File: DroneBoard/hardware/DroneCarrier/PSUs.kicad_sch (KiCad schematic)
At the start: 33 parts, among them J7 Barrel_Jack, J8 AMP171826-4, Q1 DMP3013SFV-7, U6 AP64501SP-13

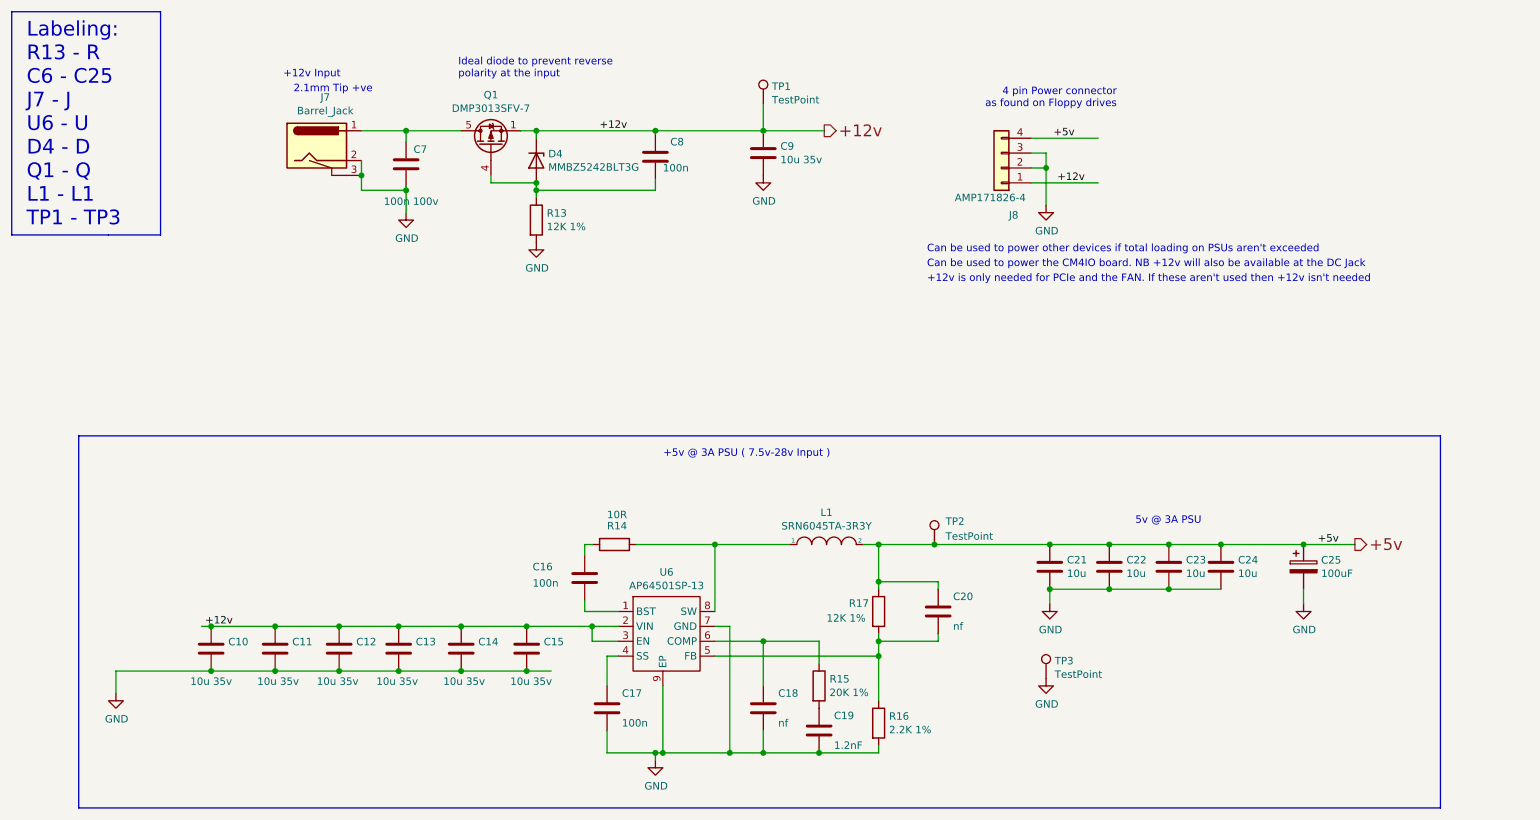
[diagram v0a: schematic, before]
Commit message: Labelling needs to be compared to the RPi CM4
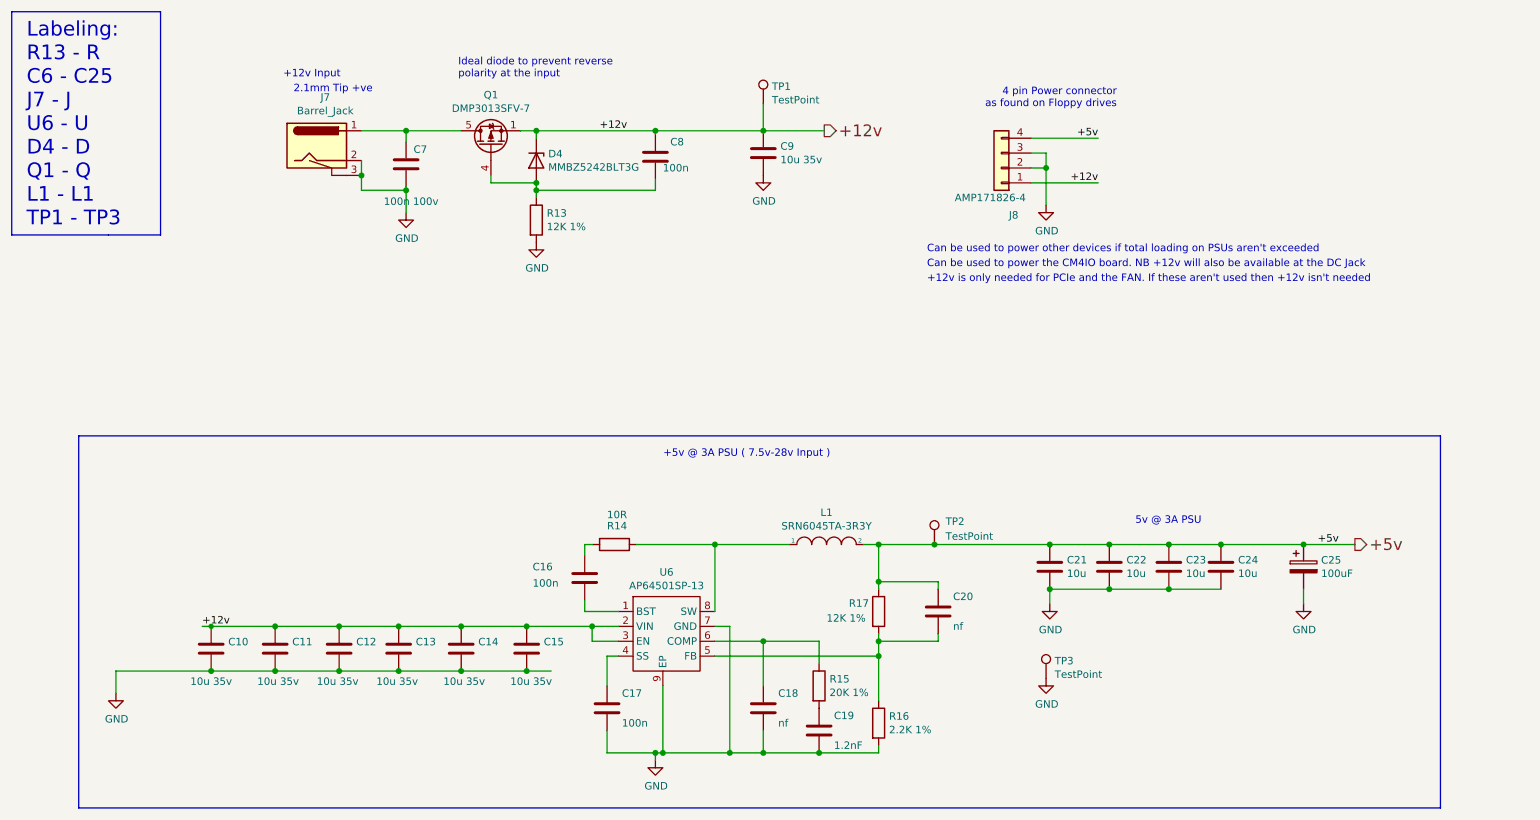
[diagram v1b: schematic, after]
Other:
- company: (none) -> Surveilia
- title: (none) -> PSU
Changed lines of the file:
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@@
 (kicad_sch (version 20210621) (generator eeschema)
   (paper "A4")
-  (junction (at 59.436 120.142) (diameter 1.016) (color 0 0 0 0))
+  (title_block
+    (title "PSU")
+    (date "2021-10-22")
+    (rev "01")
+    (company "Surveilia")
+    (comment 1 "Author: Chase W. & Kaden T.")
+  )
+  (junction (at 59.436 120.142) (diameter 0) (color 0 0 0 0))
   (junction (at 59.436 127.762) (diameter 1.016) (color 0 0 0 0))
   (junction (at 70.358 120.142) (diameter 1.016) (color 0 0 0 0))
@@
     (stroke (width 0) (type solid) (color 0 0 0 0))
   )
-  (wire (pts (xy 57.785 120.142) (xy 59.436 120.142))
-    (stroke (width 0) (type solid) (color 0 0 0 0))
+  (wire (pts (xy 57.912 120.142) (xy 59.436 120.142))
+    (stroke (width 0) (type default) (color 0 0 0 0))
   )
   (wire (pts (xy 59.436 120.142) (xy 70.358 120.142))
@@
     (effects (font (size 1.27 1.27)) (justify left bottom))
   )
-  (label "+12v" (at 58.42 120.142 0)
+  (label "+12v" (at 57.912 120.142 0)
     (effects (font (size 1.27 1.27)) (justify left bottom))
   )
@@
     (effects (font (size 1.27 1.27)) (justify left bottom))
   )
-  (label "+5v" (at 203.2 36.83 0)
-    (effects (font (size 1.27 1.27)) (justify left bottom))
-  )
-  (label "+12v" (at 203.835 44.45 0)
-    (effects (font (size 1.27 1.27)) (justify left bottom))
+  (label "+5v" (at 210.82 36.83 180)
+    (effects (font (size 1.27 1.27)) (justify right bottom))
+  )
+  (label "+12v" (at 210.82 44.45 180)
+    (effects (font (size 1.27 1.27)) (justify right bottom))
   )
   (label "+5v" (at 248.285 106.172 0)
@@
   (symbol (lib_id "power:GND") (at 43.18 131.572 0) (unit 1)
     (in_bom yes) (on_board yes)
-    (property "Reference" "#PWR?" (id 0) (at 43.18 137.922 0)
+    (property "Reference" "#PWR0114" (id 0) (at 43.18 137.922 0)
       (effects (font (size 1.27 1.27)) hide)
     )
@@
   (symbol (lib_id "power:GND") (at 92.71 49.53 0) (unit 1)
     (in_bom yes) (on_board yes)
-    (property "Reference" "#PWR?" (id 0) (at 92.71 55.88 0)
+    (property "Reference" "#PWR0116" (id 0) (at 92.71 55.88 0)
       (effects (font (size 1.27 1.27)) hide)
     )
@@
   (symbol (lib_id "power:GND") (at 114.935 54.61 0) (unit 1)
     (in_bom yes) (on_board yes)
-    (property "Reference" "#PWR?" (id 0) (at 114.935 60.96 0)
+    (property "Reference" "#PWR0108" (id 0) (at 114.935 60.96 0)
       (effects (font (size 1.27 1.27)) hide)
     )
@@
   (symbol (lib_id "power:GND") (at 135.255 143.002 0) (unit 1)
     (in_bom yes) (on_board yes)
-    (property "Reference" "#PWR?" (id 0) (at 135.255 149.352 0)
+    (property "Reference" "#PWR0113" (id 0) (at 135.255 149.352 0)
       (effects (font (size 1.27 1.27)) hide)
     )
@@
   (symbol (lib_id "power:GND") (at 153.67 43.18 0) (unit 1)
     (in_bom yes) (on_board yes)
-    (property "Reference" "#PWR?" (id 0) (at 153.67 49.53 0)
+    (property "Reference" "#PWR0109" (id 0) (at 153.67 49.53 0)
       (effects (font (size 1.27 1.27)) hide)
     )
@@
   (symbol (lib_id "power:GND") (at 201.93 48.26 0) (unit 1)
     (in_bom yes) (on_board yes)
-    (property "Reference" "#PWR?" (id 0) (at 201.93 54.61 0)
+    (property "Reference" "#PWR0107" (id 0) (at 201.93 54.61 0)
       (effects (font (size 1.27 1.27)) hide)
     )
@@
   (symbol (lib_id "power:GND") (at 201.93 129.032 0) (unit 1)
     (in_bom yes) (on_board yes)
-    (property "Reference" "#PWR?" (id 0) (at 201.93 135.382 0)
+    (property "Reference" "#PWR0115" (id 0) (at 201.93 135.382 0)
       (effects (font (size 1.27 1.27)) hide)
     )
@@
   (symbol (lib_id "power:GND") (at 202.565 116.332 0) (unit 1)
     (in_bom yes) (on_board yes)
-    (property "Reference" "#PWR?" (id 0) (at 202.565 122.682 0)
+    (property "Reference" "#PWR0104" (id 0) (at 202.565 122.682 0)
       (effects (font (size 1.27 1.27)) hide)
     )
@@
   (symbol (lib_id "power:GND") (at 245.872 116.332 0) (unit 1)
     (in_bom yes) (on_board yes)
-    (property "Reference" "#PWR?" (id 0) (at 245.872 122.682 0)
-      (effects (font (size 1.27 1.27)) hide)
-    )
+    (property "Reference" "#PWR0106" (id 0) (at 245.872 122.682 0)
+      (effects (font (size 1.27 1.27)) hide)
+    )

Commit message: Add files via upload
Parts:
- removed C10, C11, C12, C13, C14, C15, C9: 10u 35v, Capacitor_SMD:C_0805_2012Metric, symbol Device:C
- removed C16, C17, C8: 100n, Capacitor_SMD:C_0402_1005Metric, symbol Device:C
- removed C18, C20: nf, Capacitor_SMD:C_0402_1005Metric, symbol Device:C
- removed C19: 1.2nF, Capacitor_SMD:C_0402_1005Metric, symbol Device:C
- removed C21, C22, C23, C24: 10u, Capacitor_SMD:C_0805_2012Metric, symbol Device:C
- removed C25: 100uF, Capacitor_Tantalum_SMD:CP_EIA-7343-31_Kemet-D, symbol Device:CP
- removed C7: 100n 100v, Capacitor_SMD:C_0402_1005Metric, symbol Device:C
- removed D4: MMBZ5242BLT3G, Diode_SMD:D_SOT-23_ANK, symbol Diode:BZX84Cxx
- removed J8: AMP171826-4, 171826-4:TE_171826-4, symbol Connector_Generic:Conn_01x04
- removed L1: SRN6045TA-3R3Y, Inductor_SMD:L_Bourns_SRN6045TA, symbol pspice:INDUCTOR
- removed Q1: DMP3013SFV-7, Package_SON:Diodes_PowerDI3333-8, symbol Transistor_FET:DMP3013SFV
- removed R13, R17: 12K 1%, Resistor_SMD:R_0402_1005Metric, symbol Device:R
- removed R14: 10R, Resistor_SMD:R_0402_1005Metric, symbol Device:R
- removed R15: 20K 1%, Resistor_SMD:R_0402_1005Metric, symbol Device:R
- removed R16: 2.2K 1%, Resistor_SMD:R_0402_1005Metric, symbol Device:R
- removed TP1, TP2, TP3: TestPoint, TestPoint:TestPoint_Pad_2.0x2.0mm, symbol Connector:TestPoint
- removed U6: AP64501SP-13, Package_SO:SOIC-8-1EP_3.9x4.9mm_P1.27mm_EP2.95x4.9mm_Mask2.71x3.4mm_ThermalVias, symbol CM4IO:AP64351
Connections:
- net +5v: now also J7.1
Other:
- note added: "5V input"
- note added: "Labeling: J7 - J"
- note removed: "+12v Input"
- note removed: "+12v is only needed for PCIe and the FAN. If these aren't used then +12v isn't needed"
- note removed: "+5v @ 3A PSU ( 7.5v-28v Input )"
- note removed: "4 pin Power connector as found on Floppy drives"
- note removed: "5v @ 3A PSU"
- note removed: "Can be used to power other devices if total loading on PSUs aren't exceeded"
- note removed: "Can be used to power the CM4IO board. NB +12v will also be available at the DC Jack"
- note removed: "Ideal diode to prevent reverse polarity at the input"
- note removed: "Labeling: R13 - R C6 - C25 J7 - J U6 - U D4 - D Q1 - Q L1 - L1 TP1 - TP3"
